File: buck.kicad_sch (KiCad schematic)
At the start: 14 parts

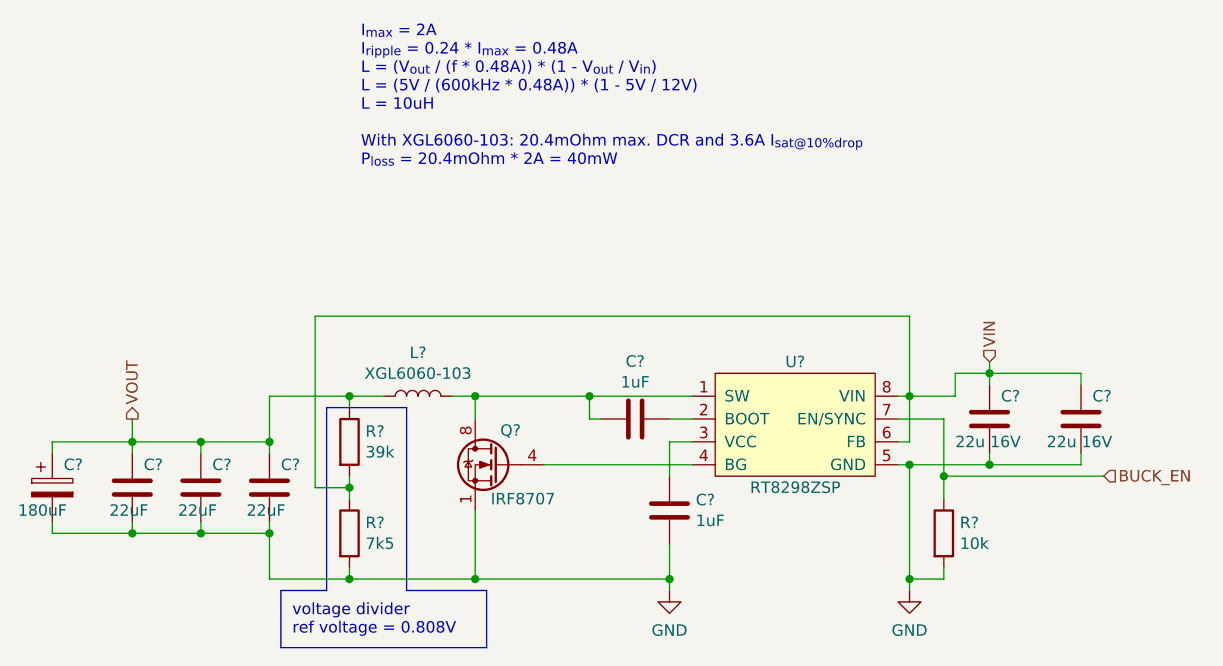
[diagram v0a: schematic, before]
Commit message: Annotate symbols and assign footprints
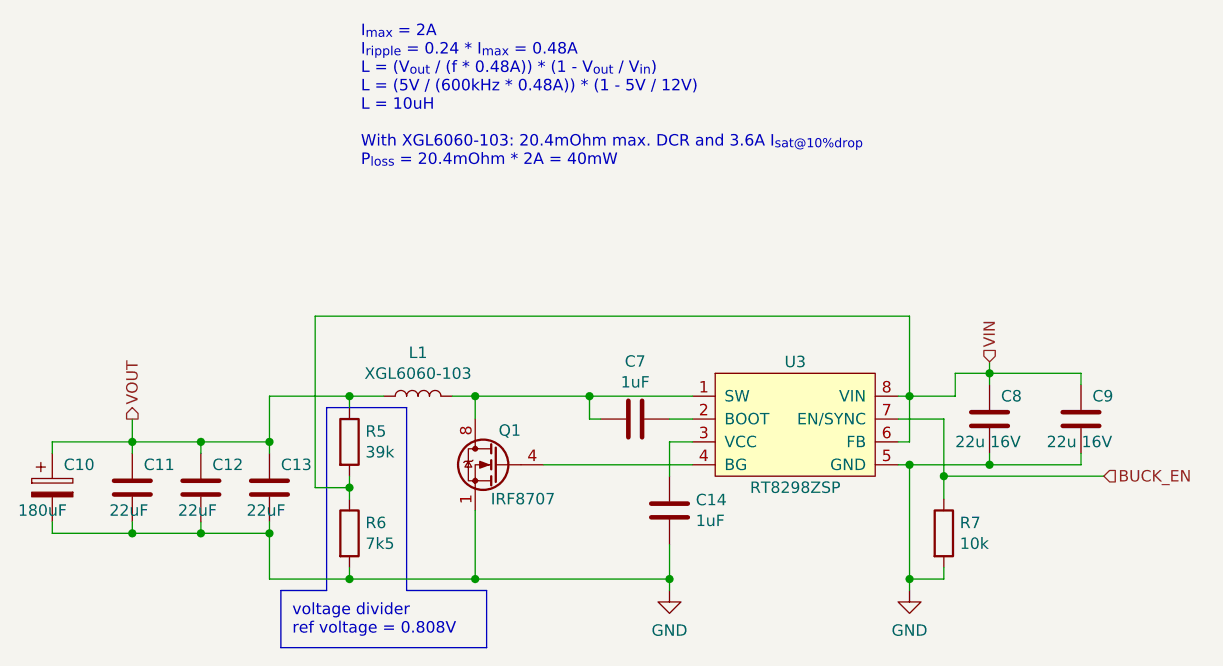
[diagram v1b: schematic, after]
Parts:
- gave numbers to parts that had none: 14
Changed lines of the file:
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@@
   (symbol (lib_id "extraSymbols:RT8298ZSP") (at 161.29 91.44 0) (unit 1)
     (in_bom yes) (on_board yes)
-    (property "Reference" "U?" (id 0) (at 161.29 83.82 0))
+    (property "Reference" "U3" (id 0) (at 161.29 83.82 0))
     (property "Value" "RT8298ZSP" (id 1) (at 161.29 97.79 0))
     (property "Footprint" "Package_SO:HSOP-8-1EP_3.9x4.9mm_P1.27mm_EP2.41x3.1mm_ThermalVias" (id 2) (at 156.21 91.44 0)
@@
   (symbol (lib_id "Device:C") (at 193.04 90.17 0) (unit 1)
     (in_bom yes) (on_board yes)
-    (property "Reference" "C?" (id 0) (at 194.31 87.63 0)
+    (property "Reference" "C9" (id 0) (at 194.31 87.63 0)
       (effects (font (size 1.27 1.27)) (justify left))
     )
@@
   (symbol (lib_id "Device:C") (at 102.87 97.79 0) (unit 1)
     (in_bom yes) (on_board yes)
-    (property "Reference" "C?" (id 0) (at 104.14 95.25 0)
+    (property "Reference" "C13" (id 0) (at 104.14 95.25 0)
       (effects (font (size 1.27 1.27)) (justify left))
     )
@@
   (symbol (lib_id "Device:C_Polarized") (at 78.74 97.79 0) (unit 1)
     (in_bom yes) (on_board yes)
-    (property "Reference" "C?" (id 0) (at 80.01 95.25 0)
+    (property "Reference" "C10" (id 0) (at 80.01 95.25 0)
       (effects (font (size 1.27 1.27)) (justify left))
     )
@@
   (symbol (lib_id "power:GND") (at 173.99 109.22 0) (unit 1)
     (in_bom yes) (on_board yes) (fields_autoplaced)
-    (property "Reference" "#PWR?" (id 0) (at 173.99 115.57 0)
+    (property "Reference" "#PWR019" (id 0) (at 173.99 115.57 0)
       (effects (font (size 1.27 1.27)) hide)
     )
@@
   (symbol (lib_id "Transistor_FET:IRF8721PBF-1") (at 128.27 95.25 0) (mirror y) (unit 1)
     (in_bom yes) (on_board yes)
-    (property "Reference" "Q?" (id 0) (at 130.81 91.44 0)
+    (property "Reference" "Q1" (id 0) (at 130.81 91.44 0)
       (effects (font (size 1.27 1.27)) (justify left))
     )
@@
   (symbol (lib_id "Device:C") (at 95.25 97.79 0) (unit 1)
     (in_bom yes) (on_board yes)
-    (property "Reference" "C?" (id 0) (at 96.52 95.25 0)
+    (property "Reference" "C12" (id 0) (at 96.52 95.25 0)
       (effects (font (size 1.27 1.27)) (justify left))
     )
@@
   (symbol (lib_id "Device:R") (at 111.76 92.71 0) (unit 1)
     (in_bom yes) (on_board yes)
-    (property "Reference" "R?" (id 0) (at 113.538 91.5416 0)
+    (property "Reference" "R5" (id 0) (at 113.538 91.5416 0)
       (effects (font (size 1.27 1.27)) (justify left))
     )
@@
   (symbol (lib_id "Device:C") (at 182.88 90.17 0) (unit 1)
     (in_bom yes) (on_board yes)
-    (property "Reference" "C?" (id 0) (at 184.15 87.63 0)
+    (property "Reference" "C8" (id 0) (at 184.15 87.63 0)
       (effects (font (size 1.27 1.27)) (justify left))
     )
@@
   (symbol (lib_id "Device:C") (at 147.32 100.33 0) (unit 1)
     (in_bom yes) (on_board yes)
-    (property "Reference" "C?" (id 0) (at 150.241 99.1616 0)
+    (property "Reference" "C14" (id 0) (at 150.241 99.1616 0)
       (effects (font (size 1.27 1.27)) (justify left))
     )
@@
   (symbol (lib_id "Device:L") (at 119.38 87.63 90) (unit 1)
     (in_bom yes) (on_board yes)
-    (property "Reference" "L?" (id 0) (at 119.38 82.804 90))
+    (property "Reference" "L1" (id 0) (at 119.38 82.804 90))
     (property "Value" "XGL6060-103" (id 1) (at 119.38 85.1154 90))
     (property "Footprint" "Inductor_SMD:L_Coilcraft_XAL60xx_6.36x6.56mm" (id 2) (at 119.38 87.63 0)
@@
   (symbol (lib_id "Device:R") (at 177.8 102.87 0) (unit 1)
     (in_bom yes) (on_board yes)
-    (property "Reference" "R?" (id 0) (at 179.578 101.7016 0)
+    (property "Reference" "R7" (id 0) (at 179.578 101.7016 0)
       (effects (font (size 1.27 1.27)) (justify left))
     )
@@
   (symbol (lib_id "Device:C") (at 143.51 90.17 270) (unit 1)
     (in_bom yes) (on_board yes)
-    (property "Reference" "C?" (id 0) (at 143.51 83.7692 90))
+    (property "Reference" "C7" (id 0) (at 143.51 83.7692 90))
     (property "Value" "1uF" (id 1) (at 143.51 86.0806 90))
     (property "Footprint" "" (id 2) (at 139.7 91.1352 0)
@@
   (symbol (lib_id "power:GND") (at 147.32 109.22 0) (unit 1)
     (in_bom yes) (on_board yes) (fields_autoplaced)
-    (property "Reference" "#PWR?" (id 0) (at 147.32 115.57 0)
+    (property "Reference" "#PWR018" (id 0) (at 147.32 115.57 0)
       (effects (font (size 1.27 1.27)) hide)
     )
@@
   (symbol (lib_id "Device:R") (at 111.76 102.87 0) (unit 1)
     (in_bom yes) (on_board yes)
-    (property "Reference" "R?" (id 0) (at 113.538 101.7016 0)
+    (property "Reference" "R6" (id 0) (at 113.538 101.7016 0)
       (effects (font (size 1.27 1.27)) (justify left))
     )
@@
   (symbol (lib_id "Device:C") (at 87.63 97.79 0) (unit 1)
     (in_bom yes) (on_board yes)
-    (property "Reference" "C?" (id 0) (at 88.9 95.25 0)
-      (effects (font (size 1.27 1.27)) (justify left))
-    )
+    (property "Reference" "C11" (id 0) (at 88.9 95.25 0)
+      (effects (font (size 1.27 1.27)) (justify left))
+    )

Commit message: Finish schematic
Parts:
- C11, C12, C13, C8, C9: footprint (none) -> Capacitor_SMD:C_0805_2012Metric
- C14, C7: footprint (none) -> Capacitor_SMD:C_0603_1608Metric
- R5, R6, R7: footprint (none) -> Resistor_SMD:R_0603_1608Metric
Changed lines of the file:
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@@
       (effects (font (size 1.27 1.27)) (justify left))
     )
-    (property "Footprint" "" (id 2) (at 194.0052 93.98 0)
+    (property "Footprint" "Capacitor_SMD:C_0805_2012Metric" (id 2) (at 194.0052 93.98 0)
       (effects (font (size 1.27 1.27)) hide)
     )
@@
       (effects (font (size 1.27 1.27)) (justify left))
     )
-    (property "Footprint" "" (id 2) (at 103.8352 101.6 0)
+    (property "Footprint" "Capacitor_SMD:C_0805_2012Metric" (id 2) (at 103.8352 101.6 0)
       (effects (font (size 1.27 1.27)) hide)
     )
@@
   (symbol (lib_id "power:GND") (at 173.99 109.22 0) (unit 1)
     (in_bom yes) (on_board yes) (fields_autoplaced)
-    (property "Reference" "#PWR019" (id 0) (at 173.99 115.57 0)
+    (property "Reference" "#PWR023" (id 0) (at 173.99 115.57 0)
       (effects (font (size 1.27 1.27)) hide)
     )
@@
       (effects (font (size 1.27 1.27)) (justify left))
     )
-    (property "Footprint" "" (id 2) (at 96.2152 101.6 0)
+    (property "Footprint" "Capacitor_SMD:C_0805_2012Metric" (id 2) (at 96.2152 101.6 0)
       (effects (font (size 1.27 1.27)) hide)
     )
@@
       (effects (font (size 1.27 1.27)) (justify left))
     )
-    (property "Footprint" "" (id 2) (at 109.982 92.71 90)
+    (property "Footprint" "Resistor_SMD:R_0603_1608Metric" (id 2) (at 109.982 92.71 90)
       (effects (font (size 1.27 1.27)) hide)
     )
@@
       (effects (font (size 1.27 1.27)) (justify left))
     )
-    (property "Footprint" "" (id 2) (at 183.8452 93.98 0)
+    (property "Footprint" "Capacitor_SMD:C_0805_2012Metric" (id 2) (at 183.8452 93.98 0)
       (effects (font (size 1.27 1.27)) hide)
     )
@@
       (effects (font (size 1.27 1.27)) (justify left))
     )
-    (property "Footprint" "" (id 2) (at 148.2852 104.14 0)
+    (property "Footprint" "Capacitor_SMD:C_0603_1608Metric" (id 2) (at 148.2852 104.14 0)
       (effects (font (size 1.27 1.27)) hide)
     )
@@
       (effects (font (size 1.27 1.27)) (justify left))
     )
-    (property "Footprint" "" (id 2) (at 176.022 102.87 90)
+    (property "Footprint" "Resistor_SMD:R_0603_1608Metric" (id 2) (at 176.022 102.87 90)
       (effects (font (size 1.27 1.27)) hide)
     )
@@
     (property "Reference" "C7" (id 0) (at 143.51 83.7692 90))
     (property "Value" "1uF" (id 1) (at 143.51 86.0806 90))
-    (property "Footprint" "" (id 2) (at 139.7 91.1352 0)
+    (property "Footprint" "Capacitor_SMD:C_0603_1608Metric" (id 2) (at 139.7 91.1352 0)
       (effects (font (size 1.27 1.27)) hide)
     )
@@
   (symbol (lib_id "power:GND") (at 147.32 109.22 0) (unit 1)
     (in_bom yes) (on_board yes) (fields_autoplaced)
-    (property "Reference" "#PWR018" (id 0) (at 147.32 115.57 0)
+    (property "Reference" "#PWR022" (id 0) (at 147.32 115.57 0)
       (effects (font (size 1.27 1.27)) hide)
     )
@@
       (effects (font (size 1.27 1.27)) (justify left))
     )
-    (property "Footprint" "" (id 2) (at 109.982 102.87 90)
+    (property "Footprint" "Resistor_SMD:R_0603_1608Metric" (id 2) (at 109.982 102.87 90)
       (effects (font (size 1.27 1.27)) hide)
     )
@@
       (effects (font (size 1.27 1.27)) (justify left))
     )
-    (property "Footprint" "" (id 2) (at 88.5952 101.6 0)
-      (effects (font (size 1.27 1.27)) hide)
-    )
+    (property "Footprint" "Capacitor_SMD:C_0805_2012Metric" (id 2) (at 88.5952 101.6 0)
+      (effects (font (size 1.27 1.27)) hide)
+    )
